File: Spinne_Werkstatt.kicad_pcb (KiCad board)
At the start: 2 copper layers, 42 x 82 mm, 17 parts, among them J1 Conn_01x02_Pin, J3 Conn_01x03_Pin, Q1 BSS138, Q2 BSS138, U1 ESP32-WROOM-32UE, U2 CH340C

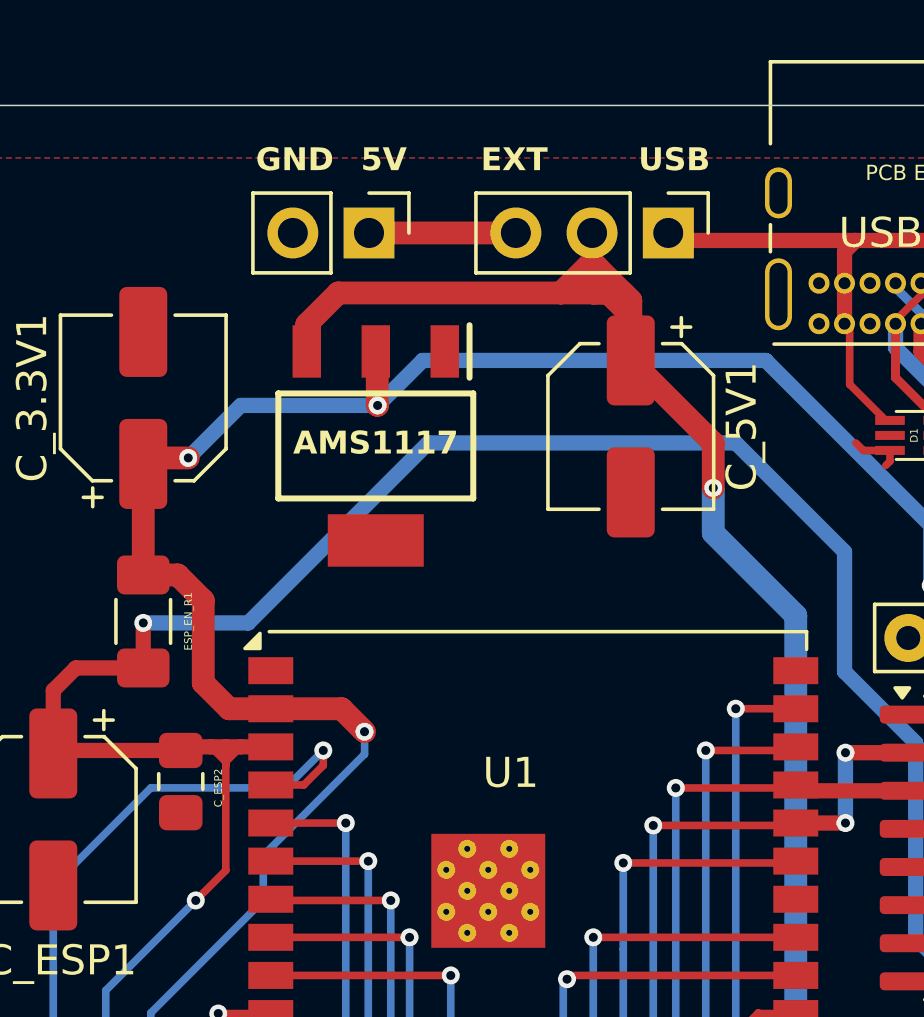
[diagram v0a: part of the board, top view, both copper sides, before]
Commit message: improved names on silkscreen  x2
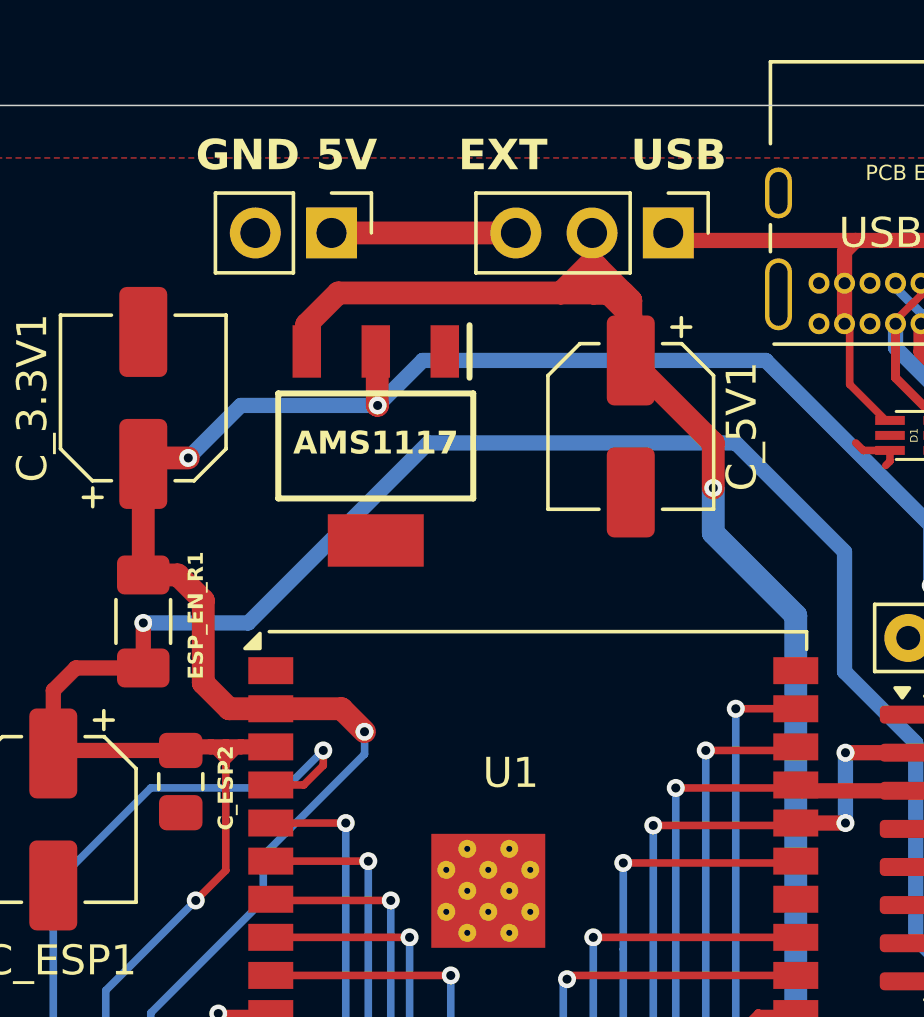
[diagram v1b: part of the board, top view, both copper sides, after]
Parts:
- moved J1 1.25 mm to (132.5, 39.8)
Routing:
- net VCC: track 4.89 -> 6.14 mm
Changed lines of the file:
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@@
 		(tags "capacitor handsolder")
 		(property "Reference" "C_ESP2"
-			(at 0.2125 -1.25 90)
+			(at 0.2125 -1.5 90)
 			(layer "F.SilkS")
 			(effects
 				(font
-					(size 0.254 0.254)
-					(thickness 0.0254)
+					(size 0.508 0.508)
+					(thickness 0.1016)
+					(bold yes)
 				)
 			)
@@
 	(footprint "Connector_PinHeader_2.54mm:PinHeader_1x02_P2.54mm_Vertical"
 		(layer "F.Cu")
-		(at 133.775 39.75 -90)
+		(at 132.525 39.75 -90)
 		(descr "Through hole straight pin header, 1x02, 2.54mm pitch, single row")
 		(tags "Through hole pin header THT 1x02 2.54mm single row")
@@
 		)
 		(property "Value" "Conn_01x02_Pin"
-			(at 0 14.62 90)
+			(at 0 1.275 0)
 			(layer "F.Fab")
 			(effects
@@
 		(tags "resistor handsolder")
 		(property "Reference" "ESP_EN_R1"
-			(at 0 -1.5 90)
+			(at -0.2 -1.75 90)
 			(layer "F.SilkS")
 			(effects
 				(font
-					(size 0.254 0.254)
-					(thickness 0.0254)
+					(size 0.508 0.508)
+					(thickness 0.1016)
+					(bold yes)
 				)
 			)
@@
 	)
 	(gr_text "USB"
-		(at 142.75 37.75 0)
+		(at 142.5 37.75 0)
 		(layer "F.SilkS")
 		(effects
 			(font
-				(size 0.762 0.762)
-				(thickness 0.127)
+				(size 1.016 1.016)
+				(thickness 0.2032)
 				(bold yes)
 			)
@@
 	)
 	(gr_text "EXT"
-		(at 137.5 37.75 0)
+		(at 136.75 37.75 0)
 		(layer "F.SilkS")
 		(effects
 			(font
-				(size 0.762 0.762)
-				(thickness 0.127)
+				(size 1.016 1.016)
+				(thickness 0.2032)
 				(bold yes)
 			)
@@
 	)
 	(gr_text "5V\n"
-		(at 133.5 37.75 0)
+		(at 132 37.75 0)
 		(layer "F.SilkS")
 		(effects
 			(font
-				(size 0.762 0.762)
-				(thickness 0.127)
+				(size 1.016 1.016)
+				(thickness 0.2032)
 				(bold yes)
 			)
@@
 	)
 	(gr_text "GND\n"
-		(at 130 37.75 0)
+		(at 128 37.75 0)
 		(layer "F.SilkS")
 		(effects
 			(font
-				(size 0.762 0.762)
-				(thickness 0.127)
+				(size 1.016 1.016)
+				(thickness 0.2032)
 				(bold yes)
 			)
@@
 	)
 	(segment
-		(start 133.775 39.75)
-		(end 138.67 39.75)
+		(start 138.67 39.75)
+		(end 132.525 39.75)
 		(width 0.762)
 		(layer "F.Cu")

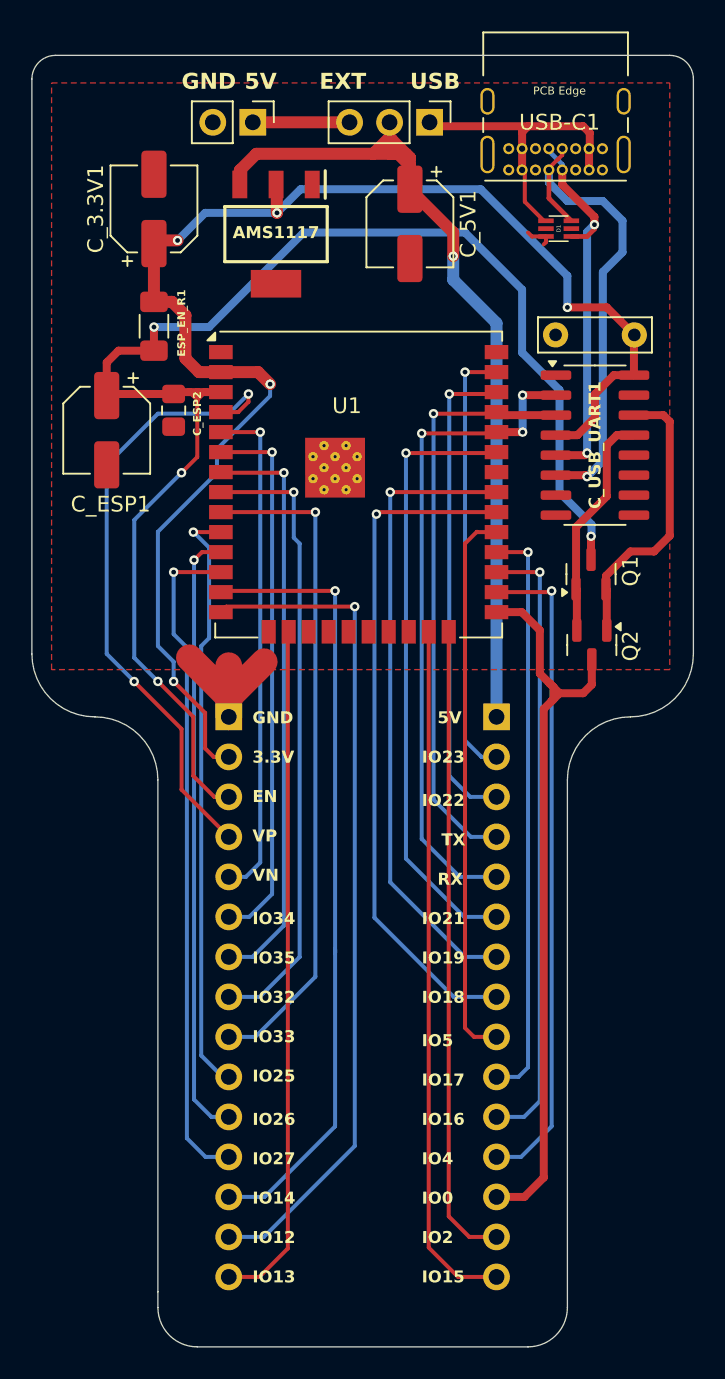
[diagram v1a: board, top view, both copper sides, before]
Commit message: added additional USB data protection, not pretty -- version 1.1.3
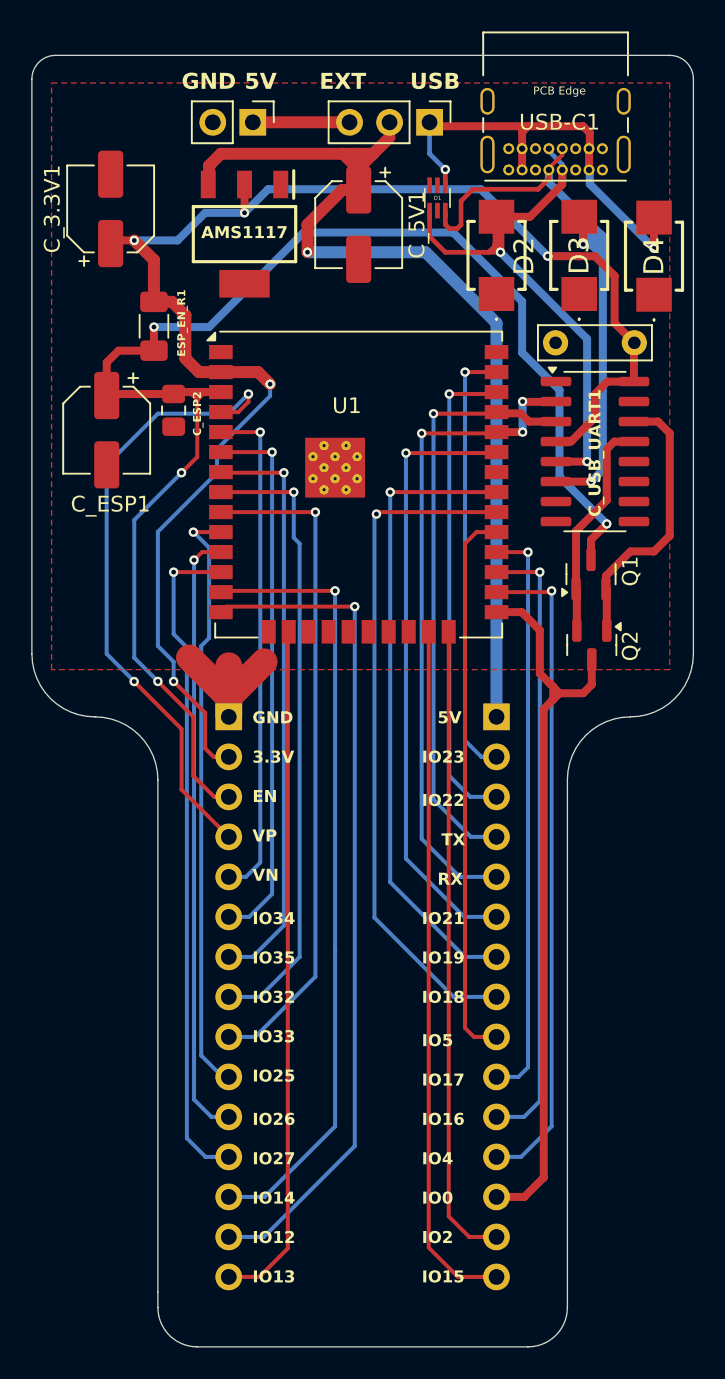
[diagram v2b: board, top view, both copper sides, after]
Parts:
- added D2: TPSMB1805CA, bulme_footprints:TPSMB1805CA, F.Cu at (148.0, 48.2)
- added D3: TPSMB1805CA, bulme_footprints:TPSMB1805CA, F.Cu at (153.2, 48.2)
- added D4: TPSMB1805CA, bulme_footprints:TPSMB1805CA, F.Cu at (158.0, 48.2)
- moved D1 7.94 mm to (144.2, 44.6), turned to 0 degrees
- moved C_5V1 3.25 mm to (139.2, 46.2)
- moved C_3.3V1 2.75 mm to (123.5, 45.2)
- moved AMS1117 2.00 mm to (132.0, 46.9)
- moved C_USB_UART1 0.50 mm to (156.8, 53.8)
- moved U2 0.41 mm to (154.2, 60.7)
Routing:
- net D-: track 31.3 -> 46.8 mm, vias 1 -> 2
- net D+: track 24.7 -> 37.2 mm
- net VBUS: track 19.6 -> 29.0 mm, vias 0 -> 2
- net +5V: track 56.4 -> 64.8 mm
- net +3V3: track 93.6 -> 97.5 mm
- net GND: track 11.8 -> 10.0 mm
- net Net-(Q1-S): track 18.3 -> 17.7 mm
